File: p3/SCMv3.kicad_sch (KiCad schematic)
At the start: 126 parts, among them IC1 40106, IC2 40106, IC3 TL082, J1 Conn_01x06, J1-OUT8 JACK-MONO-SWB, J2 Conn_01x02, J2-OUT7 JACK-MONO-SWB, J3 POWER, J3-OUT6 JACK-MONO-SWB, J4 Conn_01x02, J4-OUT5 JACK-MONO-SWB, J5-OUT4 JACK-MONO-SWB, J6-OUT3 JACK-MONO-SWB, J7-OUT2 JACK-MONO-SWB, J8-OUT1 JACK-MONO-SWB, J9-CLK_IN1 JCLK_IN, Q1 Si2318, Q2 Si2318, Q3 Si2318, Q4 Si2318, U1 STM32F030K6Tx, U2 AP7384-33, Y1 16MHz_18pF_FA238

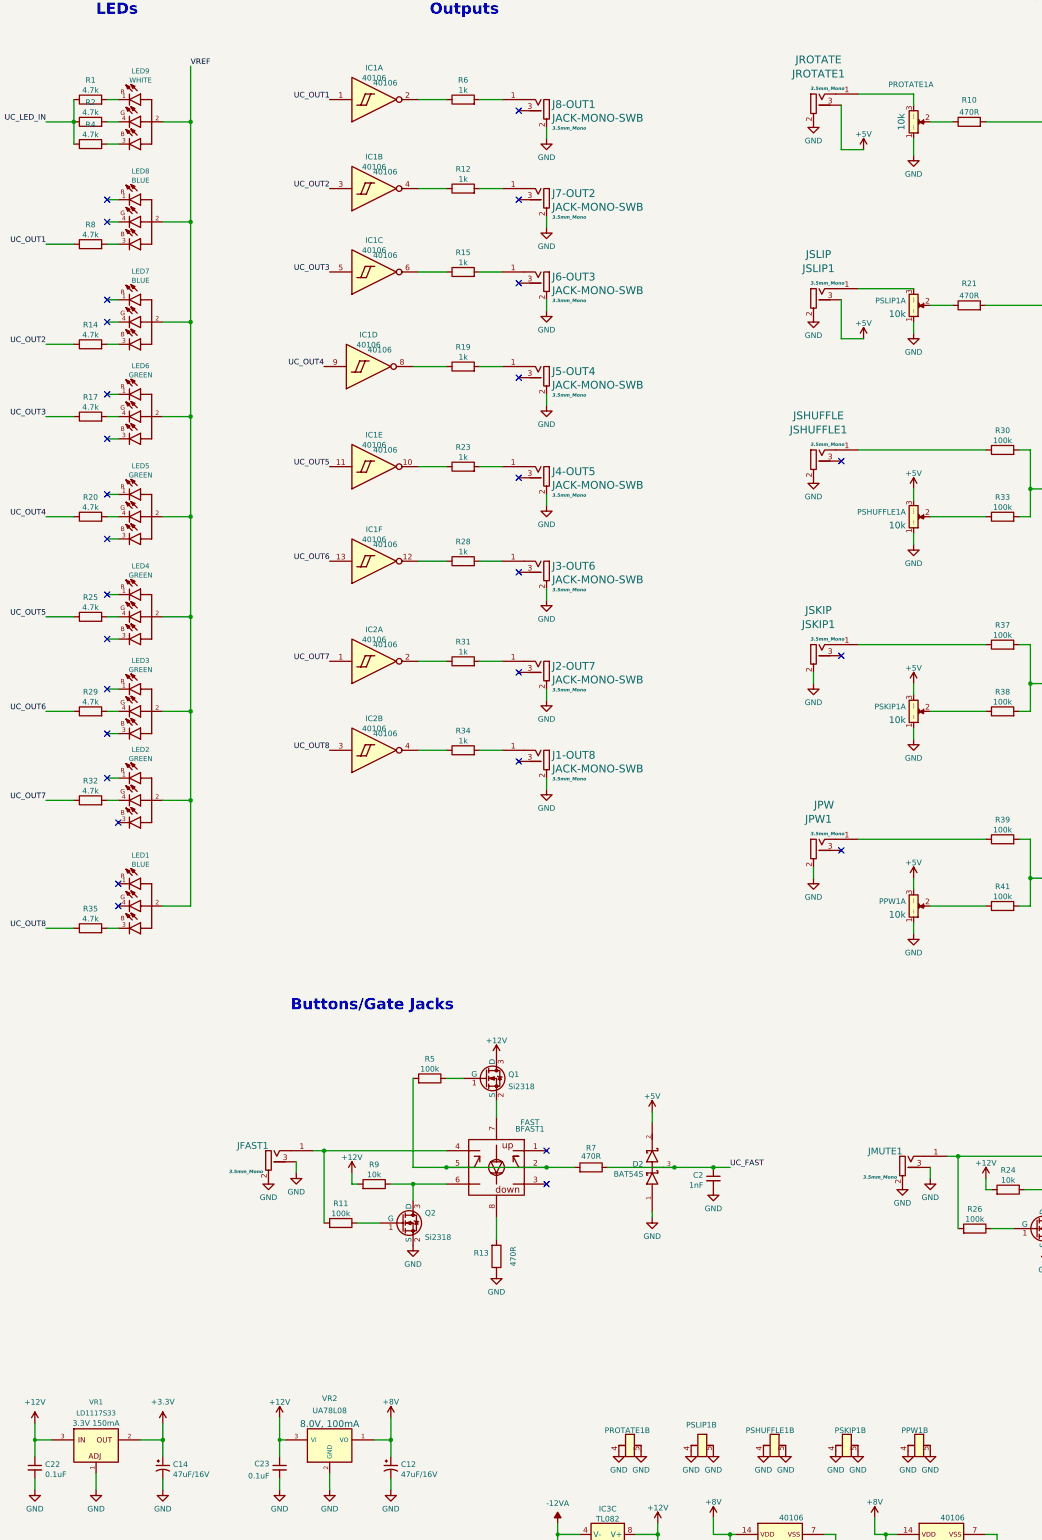
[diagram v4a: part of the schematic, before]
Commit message: Fixed errors on pcb and schem
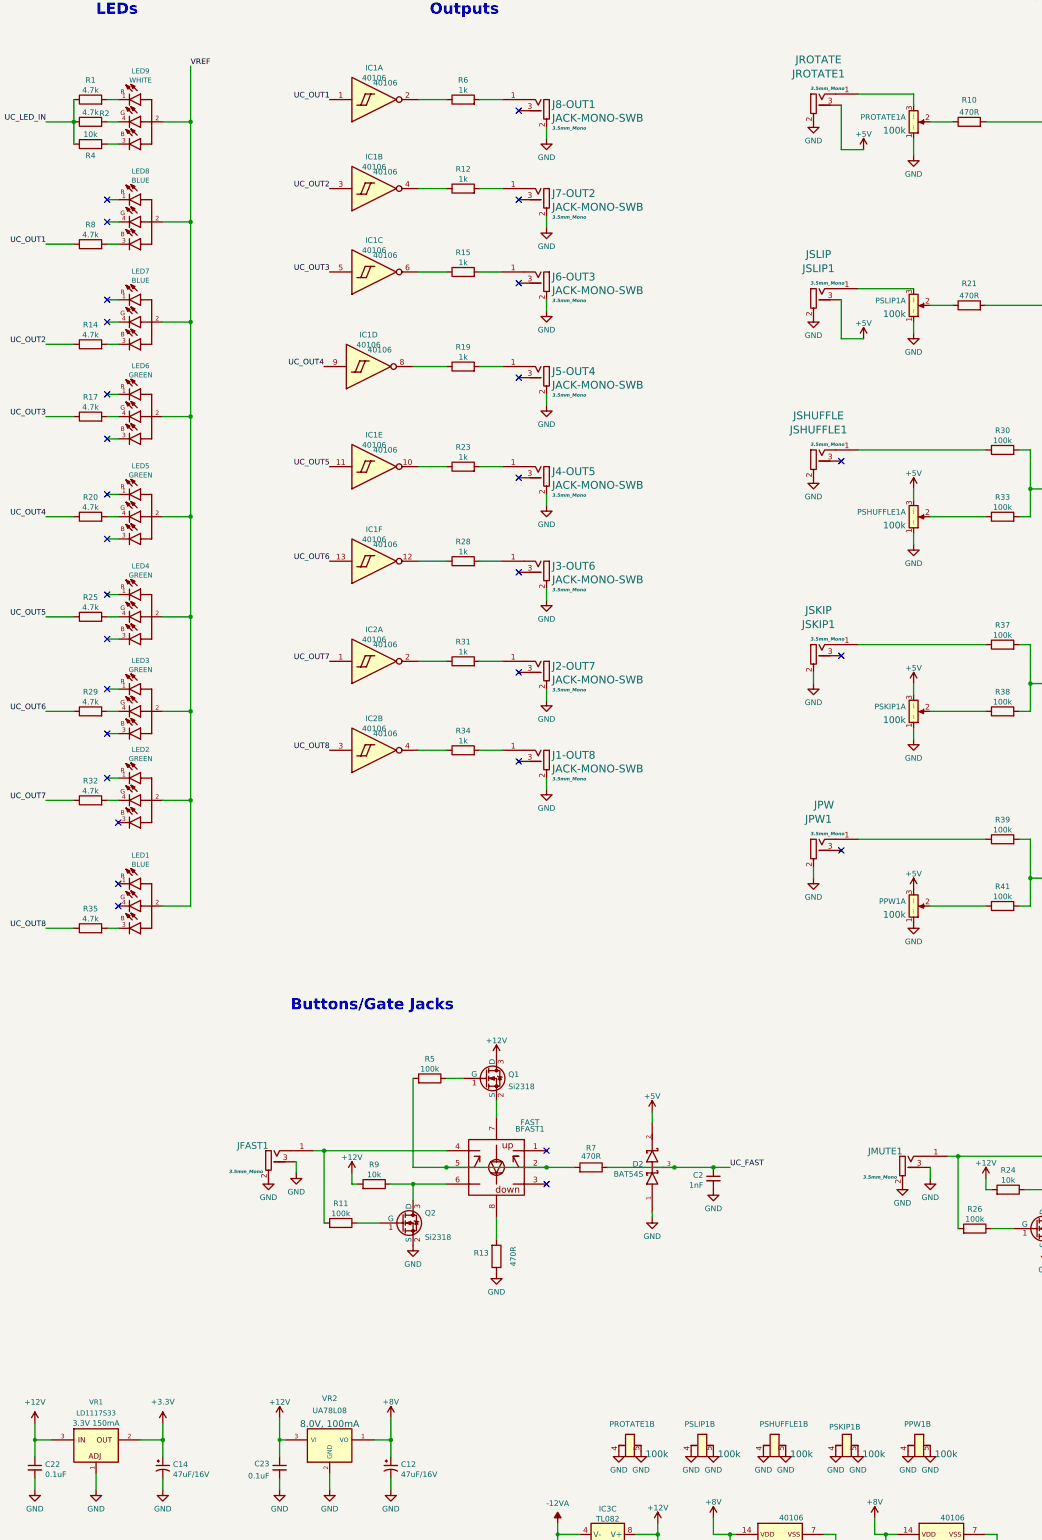
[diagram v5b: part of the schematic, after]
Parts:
- removed PPW1, PROTATE1, PSHUFFLE1, PSKIP1, PSLIP1: 9mm_CtrDet_10k_DShaft, 4ms_Potentiometer:Pot_9mm_Dshaft_Det, symbol 4ms_Potentiometer:9mm_CtrDet_10k_DShaft
- removed R4: 4.7k_0603, 4ms_Resistor:R_0603, symbol 4ms_Resistor:4.7k_0603
- added PPW1, PROTATE1, PSHUFFLE1, PSKIP1, PSLIP1: 9mm_NoDet_100k_Knurled_Lined, 4ms_Potentiometer:Pot_9mm_Knurl_NoDet, symbol 4ms_Potentiometer:9mm_NoDet_100k_Knurled_Lined
- added R4: 10k_0603, 4ms_Resistor:R_0603, symbol 4ms_Resistor:10k_0603
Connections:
- net +5V: now also PPW1.3 (Right), PSHUFFLE1.3 (Right), PSKIP1.3 (Right)
- net GND: now also PPW1.1 (Left), PPW1.4 (Tab1), PPW1.5 (Tab2), PROTATE1.1 (Left), PROTATE1.4 (Tab1), PROTATE1.5 (Tab2), PSHUFFLE1.1 (Left), PSHUFFLE1.4 (Tab1), PSHUFFLE1.5 (Tab2), PSKIP1.1 (Left), PSKIP1.4 (Tab1), PSKIP1.5 (Tab2), PSLIP1.1 (Left), PSLIP1.4 (Tab1), PSLIP1.5 (Tab2)
- net UC_LED_IN: now also R4.1
- net at R33.1: now also PSHUFFLE1.2 (Center)
- net at LED9.3 (CB): now also R4.2
- net at R38.1: now also PSKIP1.2 (Center)
- net at R41.1: now also PPW1.2 (Center)
- net at R21.1: now also PSLIP1.2 (Center)
- net at JSLIP1.1 (SIG): now also PSLIP1.3 (Right)
- net at JROTATE1.1 (SIG): now also PROTATE1.3 (Right)
- net at R10.1: now also PROTATE1.2 (Center)

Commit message: fixed routing error
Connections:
- net SWCLK: now also U1.24 (PA14); no longer U1.23 (PA13)
- net SWDIO: now also U1.23 (PA13); no longer U1.22 (PA12)
- net UC_CLK_IN: now also U1.22 (PA12); no longer U1.24 (PA14)
